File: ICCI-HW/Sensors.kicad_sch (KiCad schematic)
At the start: 20 parts

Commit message: usb PD started
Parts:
- R? (x2): value R -> 4.7k
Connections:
- net +3V3: no longer C?.1, C?.1
- net GND: now also U?.3 (GND), U?.5 (PGND)
- net SCL: now also U?.2 (SCL)
- net SDA: now also U?.8 (SDA)
- net +1V8: now reaches U?.1 (VDD)
- net +1V8: now also C?.1, C?.1
- no-connect marks 0 -> 2
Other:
- note added: "SDA, SCL, INT, LDR are 3V3 tolerant"
- note removed: "1.8V !!!"
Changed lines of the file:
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@@
   (junction (at 161.925 70.485) (diameter 0) (color 0 0 0 0)
   )
+  (junction (at 169.545 95.885) (diameter 0) (color 0 0 0 0)
+  )
   (junction (at 151.13 141.605) (diameter 0) (color 0 0 0 0)
   )
@@
   (junction (at 166.37 80.01) (diameter 0) (color 0 0 0 0)
   )
+  (junction (at 166.37 93.345) (diameter 0) (color 0 0 0 0)
+  )
   (junction (at 134.62 98.425) (diameter 0) (color 0 0 0 0)
   )
+  (junction (at 134.62 120.65) (diameter 0) (color 0 0 0 0)
+  )
+  (no_connect (at 156.21 113.03))
+  (no_connect (at 156.21 110.49))
   (wire (pts (xy 161.925 70.485) (xy 161.925 47.625))
     (stroke (width 0) (type default) (color 0 0 0 0))
@@
     (stroke (width 0) (type default) (color 0 0 0 0))
   )
+  (wire (pts (xy 135.89 120.65) (xy 134.62 120.65))
+    (stroke (width 0) (type default) (color 0 0 0 0))
+  )
   (wire (pts (xy 166.37 59.055) (xy 168.275 59.055))
     (stroke (width 0) (type default) (color 0 0 0 0))
@@
     (stroke (width 0) (type default) (color 0 0 0 0))
   )
+  (wire (pts (xy 156.21 115.57) (xy 166.37 115.57))
+    (stroke (width 0) (type default) (color 0 0 0 0))
+  )
   (wire (pts (xy 166.37 80.01) (xy 161.925 80.01))
     (stroke (width 0) (type default) (color 0 0 0 0))
@@
     (stroke (width 0) (type default) (color 0 0 0 0))
   )
+  (wire (pts (xy 166.37 115.57) (xy 166.37 93.345))
+    (stroke (width 0) (type default) (color 0 0 0 0))
+  )
+  (wire (pts (xy 134.62 118.11) (xy 134.62 120.65))
+    (stroke (width 0) (type default) (color 0 0 0 0))
+  )
   (wire (pts (xy 156.21 73.025) (xy 159.385 73.025))
     (stroke (width 0) (type default) (color 0 0 0 0))
@@
     (stroke (width 0) (type default) (color 0 0 0 0))
   )
+  (wire (pts (xy 134.62 115.57) (xy 135.89 115.57))
+    (stroke (width 0) (type default) (color 0 0 0 0))
+  )
   (wire (pts (xy 151.13 140.97) (xy 151.13 141.605))
     (stroke (width 0) (type default) (color 0 0 0 0))
@@
     (stroke (width 0) (type default) (color 0 0 0 0))
   )
+  (wire (pts (xy 169.545 118.11) (xy 169.545 95.885))
+    (stroke (width 0) (type default) (color 0 0 0 0))
+  )
+  (wire (pts (xy 134.62 114.935) (xy 134.62 115.57))
+    (stroke (width 0) (type default) (color 0 0 0 0))
+  )
   (wire (pts (xy 135.89 75.565) (xy 134.62 75.565))
     (stroke (width 0) (type default) (color 0 0 0 0))
@@
     (stroke (width 0) (type default) (color 0 0 0 0))
   )
+  (wire (pts (xy 135.89 118.11) (xy 134.62 118.11))
+    (stroke (width 0) (type default) (color 0 0 0 0))
+  )
   (wire (pts (xy 147.32 141.605) (xy 151.13 141.605))
     (stroke (width 0) (type default) (color 0 0 0 0))
@@
     (stroke (width 0) (type default) (color 0 0 0 0))
   )
+  (wire (pts (xy 134.62 120.65) (xy 134.62 121.285))
+    (stroke (width 0) (type default) (color 0 0 0 0))
+  )
   (wire (pts (xy 168.275 57.785) (xy 168.275 59.055))
     (stroke (width 0) (type default) (color 0 0 0 0))
@@
     (stroke (width 0) (type default) (color 0 0 0 0))
   )
+  (wire (pts (xy 156.21 118.11) (xy 169.545 118.11))
+    (stroke (width 0) (type default) (color 0 0 0 0))
+  )
   (wire (pts (xy 156.21 50.165) (xy 159.385 50.165))
     (stroke (width 0) (type default) (color 0 0 0 0))
@@
     (stroke (width 0) (type default) (color 0 0 0 0))
   )
-  (text "RGB + C" (at 182.88 46.355 0)
+  (text "RGB + C" (at 175.895 48.895 0)
     (effects (font (size 1.27 1.27)) (justify left bottom))
   )
-  (text "C" (at 184.785 73.025 0)
+  (text "C" (at 178.435 71.755 0)
     (effects (font (size 1.27 1.27)) (justify left bottom))
   )
-  (text "IR + IR&C" (at 184.785 94.615 0)
+  (text "IR + IR&C" (at 173.99 93.98 0)
+    (effects (font (size 1.27 1.27)) (justify left bottom))
+  )
+  (text "SDA, SCL, INT, LDR are 3V3 tolerant" (at 131.445 129.54 0)
     (effects (font (size 1.27 1.27)) (justify left bottom))
   )
@@
   (text "SENSORS" (at 147.955 33.02 180)
     (effects (font (size 3 3) (thickness 0.6) bold) (justify right bottom))
-  )
-  (text "1.8V !!!" (at 164.465 114.935 0)
-    (effects (font (size 1.27 1.27)) (justify left bottom))
   )
   (global_label "DQ" (shape bidirectional) (at 175.26 141.605 0) (fields_autoplaced)
@@
     (pin "1")
   )
-  (symbol (lib_id "power:+3V3") (at 118.745 113.03 0) (unit 1)
+  (symbol (lib_id "power:+1V8") (at 118.745 113.03 0) (unit 1)
     (in_bom yes) (on_board yes)
     (property "Reference" "#PWR?" (id 0) (at 118.745 116.84 0)
       (effects (font (size 1.27 1.27)) hide)
     )
-    (property "Value" "+3V3" (id 1) (at 118.745 109.22 0))
+    (property "Value" "+1V8" (id 1) (at 118.11 109.22 0))
     (property "Footprint" "" (id 2) (at 118.745 113.03 0)
       (effects (font (size 1.27 1.27)) hide)
@@
   (symbol (lib_id "Device:R") (at 166.37 73.66 0) (unit 1)
     (in_bom yes) (on_board yes)
-    (property "Reference" "R?" (id 0) (at 162.56 72.39 0)
-      (effects (font (size 1.27 1.27)) (justify left))
-    )
-    (property "Value" "R" (id 1) (at 162.56 74.93 0)
+    (property "Reference" "R?" (id 0) (at 163.83 69.85 0)
+      (effects (font (size 1.27 1.27)) (justify left))
+    )
+    (property "Value" "4.7k" (id 1) (at 163.83 75.565 90)
       (effects (font (size 1.27 1.27)) (justify left))
     )
@@
     (pin "1")
   )
+  (symbol (lib_id "power:GND") (at 134.62 121.285 0) (unit 1)
+    (in_bom yes) (on_board yes) (fields_autoplaced)
+    (property "Reference" "#PWR?" (id 0) (at 134.62 127.635 0)
+      (effects (font (size 1.27 1.27)) hide)
+    )
+    (property "Value" "GND" (id 1) (at 134.62 125.73 0))
+    (property "Footprint" "" (id 2) (at 134.62 121.285 0)
+      (effects (font (size 1.27 1.27)) hide)
+    )
+    (property "Datasheet" "" (id 3) (at 134.62 121.285 0)
+      (effects (font (size 1.27 1.27)) hide)
+    )
+    (pin "1")
+  )
   (symbol (lib_id "power:GND") (at 118.745 76.835 0) (unit 1)
     (in_bom yes) (on_board yes)
@@
     (pin "1")
     (pin "2")
+  )
+  (symbol (lib_id "power:+1V8") (at 134.62 114.935 0) (unit 1)
+    (in_bom yes) (on_board yes)
+    (property "Reference" "#PWR?" (id 0) (at 134.62 118.745 0)
+      (effects (font (size 1.27 1.27)) hide)
+    )
+    (property "Value" "+1V8" (id 1) (at 133.985 111.125 0))
+    (property "Footprint" "" (id 2) (at 134.62 114.935 0)
+      (effects (font (size 1.27 1.27)) hide)
+    )
+    (property "Datasheet" "" (id 3) (at 134.62 114.935 0)
+      (effects (font (size 1.27 1.27)) hide)
+    )
+    (pin "1")
   )
   (symbol (lib_id "power:+3V3") (at 118.745 69.215 0) (unit 1)
@@
     (pin "2")
   )
-  (symbol (lib_id "power:+3V3") (at 125.095 113.03 0) (unit 1)
+  (symbol (lib_id "power:+1V8") (at 125.095 113.03 0) (unit 1)
     (in_bom yes) (on_board yes)
     (property "Reference" "#PWR?" (id 0) (at 125.095 116.84 0)
       (effects (font (size 1.27 1.27)) hide)
     )
-    (property "Value" "+3V3" (id 1) (at 125.095 109.22 0))
+    (property "Value" "+1V8" (id 1) (at 124.46 109.22 0))
     (property "Footprint" "" (id 2) (at 125.095 113.03 0)
       (effects (font (size 1.27 1.27)) hide)
@@
   )
   (symbol (lib_id "Device:R") (at 169.545 73.66 0) (unit 1)
-    (in_bom yes) (on_board yes) (fields_autoplaced)
-    (property "Reference" "R?" (id 0) (at 172.085 72.3899 0)
-      (effects (font (size 1.27 1.27)) (justify left))
-    )
-    (property "Value" "R" (id 1) (at 172.085 74.9299 0)
-      (effects (font (size 1.27 1.27)) (justify left))
-    )
+    (in_bom yes) (on_board yes)
+    (property "Reference" "R?" (id 0) (at 170.18 69.85 0)
+      (effects (font (size 1.27 1.27)) (justify left))
+    )
+    (property "Value" "4.7k" (id 1) (at 172.085 75.565 90)
+      (effects (font (size 1.27 1.27)) (justify left))
+    )

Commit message: updated
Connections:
- net DQ renamed DS_DQ
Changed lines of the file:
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@@
     (stroke (width 0) (type default) (color 0 0 0 0))
   )
-  (wire (pts (xy 151.13 141.605) (xy 175.26 141.605))
+  (wire (pts (xy 151.13 141.605) (xy 172.085 141.605))
     (stroke (width 0) (type default) (color 0 0 0 0))
   )
@@
     (effects (font (size 3 3) (thickness 0.6) bold) (justify right bottom))
   )
-  (global_label "DQ" (shape bidirectional) (at 175.26 141.605 0) (fields_autoplaced)
+  (hierarchical_label "SDA" (shape bidirectional) (at 173.99 82.55 0)
     (effects (font (size 1.27 1.27)) (justify left))
-    (property "Intersheet References" "${INTERSHEET_REFS}" (id 0) (at 180.2736 141.5256 0)
-      (effects (font (size 1.27 1.27)) (justify left) hide)
-    )
   )
-  (global_label "SCL" (shape input) (at 173.99 80.01 0) (fields_autoplaced)
+  (hierarchical_label "SCL" (shape input) (at 173.99 80.01 0)
     (effects (font (size 1.27 1.27)) (justify left))
-    (property "Intersheet References" "${INTERSHEET_REFS}" (id 0) (at 179.9107 79.9306 0)
-      (effects (font (size 1.27 1.27)) (justify left) hide)
-    )
   )
-  (global_label "SDA" (shape bidirectional) (at 173.99 82.55 0) (fields_autoplaced)
+  (hierarchical_label "DS_DQ" (shape bidirectional) (at 172.085 141.605 0)
     (effects (font (size 1.27 1.27)) (justify left))
-    (property "Intersheet References" "${INTERSHEET_REFS}" (id 0) (at 179.9712 82.4706 0)
-      (effects (font (size 1.27 1.27)) (justify left) hide)
-    )
   )
   (symbol (lib_id "power:GND") (at 125.095 53.975 0) (unit 1)

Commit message: updated
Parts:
- removed JP? (x2): SolderJumper_2_Bridged, symbol Jumper:SolderJumper_2_Bridged
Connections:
- net +3V3: now also R?.1, R?.1
- net SCL renamed SCL0
- net SDA renamed SDA0
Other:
- moved on the sheet: R?

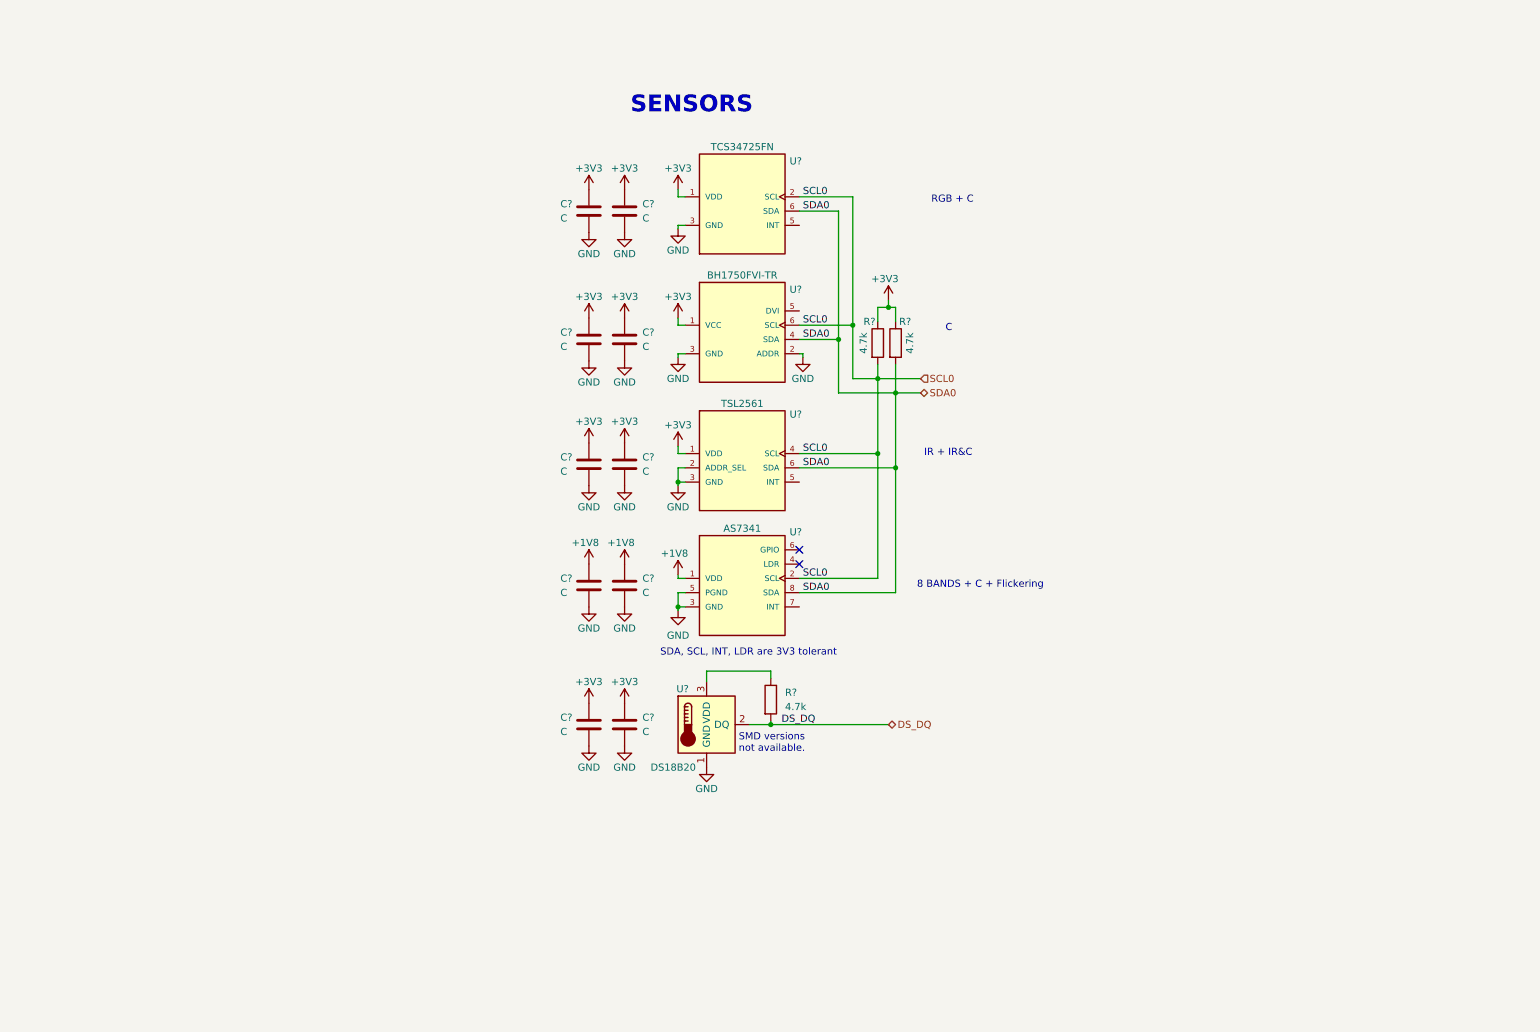
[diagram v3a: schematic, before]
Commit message: add GPIO Expansion
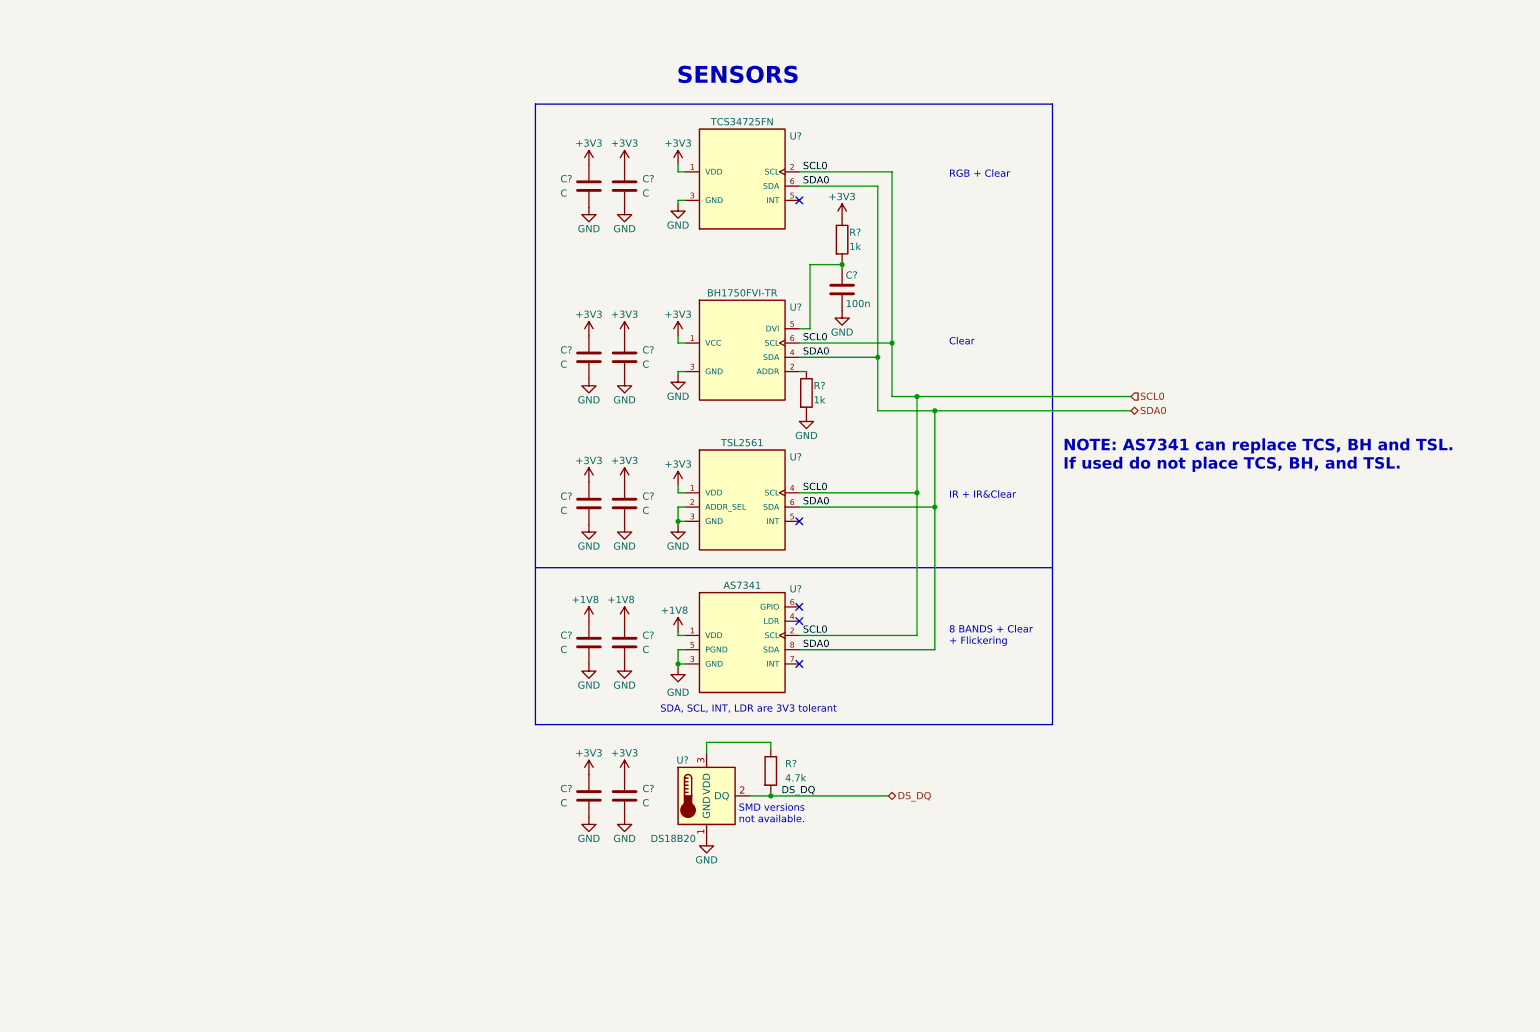
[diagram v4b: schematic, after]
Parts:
- removed R? (x2): 4.7k, symbol Device:R
- added C?: 100n, symbol Device:C
- added R? (x2): 1k, symbol Device:R
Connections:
- net +3V3: now also R?.1
- net GND: now also C?.2, R?.2; no longer U?.2 (ADDR)
- net at U?.5 (DVI): now also C?.1, R?.2
- new net: R?.1, U?.2 (ADDR)
- no-connect marks 2 -> 5
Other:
- note added: "8 BANDS + Clear + Flickering"
- note added: "Clear"
- note added: "IR + IR&Clear"
- note added: "NOTE: AS7341 can replace TCS, BH and TSL. If used do not place TCS, BH, and TSL."
- note added: "RGB + Clear"
- note removed: "8 BANDS + C + Flickering"
- note removed: "C"
- note removed: "IR + IR&C"
- note removed: "RGB + C"
- moved on the sheet: C?, R?, U?

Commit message: updated
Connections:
- net +3V3: now also R?.1, U?.3 (VDD)
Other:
- note added: "NOTE: DS18B20 Driver is using RMT ESP peripheral in order to properly handle OneWire bus without bit banding (available via IO MUX through every GPIO pin)"
- moved on the sheet: C?, R?, U?

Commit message: schematic V1.0
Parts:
- C301: renamed from C?; value C -> 4,7u
- C302, C303, C304, C305: renamed from C?; value C -> 1u
- C306, C307, C308, C309, C310: renamed from C?; value C -> 100n
- gave numbers to parts that had none: 9

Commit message: footprint assigned
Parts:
- C301, C302, C303, C304, C305, C306, C307, C308, C309, C310, C311: footprint (none) -> Capacitor_SMD:C_0603_1608Metric
- R301, R302, R303: footprint (none) -> Resistor_SMD:R_0603_1608Metric
- U302: footprint (none) -> ICCI-LIB:BH1750FVI-TR
- U303: footprint (none) -> ICCI-LIB:TCS34725FN
- U304: footprint (none) -> ICCI-LIB:TLS2561
- U305: footprint (none) -> ICCI-LIB:AS7431
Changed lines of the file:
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@@
       (effects (font (size 1.27 1.27)) (justify left))
     )
-    (property "Footprint" "" (id 2) (at 69.342 76.835 90)
+    (property "Footprint" "Resistor_SMD:R_0603_1608Metric" (id 2) (at 69.342 76.835 90)
       (effects (font (size 1.27 1.27)) hide)
     )
@@
     (property "Reference" "U303" (id 0) (at 70.485 31.115 0))
     (property "Value" "TCS34725FN" (id 1) (at 59.69 28.575 0))
-    (property "Footprint" "" (id 2) (at 59.69 37.465 0)
+    (property "Footprint" "ICCI-LIB:TCS34725FN" (id 2) (at 59.69 37.465 0)
       (effects (font (size 1.27 1.27)) (justify left bottom) hide)
     )
@@
       (effects (font (size 1.27 1.27)) (justify left))
     )
-    (property "Footprint" "" (id 2) (at 39.7002 125.095 0)
+    (property "Footprint" "Capacitor_SMD:C_0603_1608Metric" (id 2) (at 39.7002 125.095 0)
       (effects (font (size 1.27 1.27)) hide)
     )
@@
       (effects (font (size 1.27 1.27)) (justify left))
     )
-    (property "Footprint" "" (id 2) (at 33.3502 100.33 0)
+    (property "Footprint" "Capacitor_SMD:C_0603_1608Metric" (id 2) (at 33.3502 100.33 0)
       (effects (font (size 1.27 1.27)) hide)
     )
@@
       (effects (font (size 1.27 1.27)) (justify left))
     )
-    (property "Footprint" "" (id 2) (at 33.3502 74.295 0)
+    (property "Footprint" "Capacitor_SMD:C_0603_1608Metric" (id 2) (at 33.3502 74.295 0)
       (effects (font (size 1.27 1.27)) hide)
     )
@@
       (effects (font (size 1.27 1.27)) (justify left))
     )
-    (property "Footprint" "" (id 2) (at 75.692 49.53 90)
+    (property "Footprint" "Resistor_SMD:R_0603_1608Metric" (id 2) (at 75.692 49.53 90)
       (effects (font (size 1.27 1.27)) hide)
     )
@@
       (effects (font (size 1.27 1.27)) (justify left))
     )
-    (property "Footprint" "" (id 2) (at 39.7002 43.815 0)
+    (property "Footprint" "Capacitor_SMD:C_0603_1608Metric" (id 2) (at 39.7002 43.815 0)
       (effects (font (size 1.27 1.27)) hide)
     )
@@
       (effects (font (size 1.27 1.27)) (justify left))
     )
-    (property "Footprint" "" (id 2) (at 39.7002 74.295 0)
+    (property "Footprint" "Capacitor_SMD:C_0603_1608Metric" (id 2) (at 39.7002 74.295 0)
       (effects (font (size 1.27 1.27)) hide)
     )
@@
     (property "Reference" "U305" (id 0) (at 70.485 111.76 0))
     (property "Value" "AS7341" (id 1) (at 59.69 111.125 0))
-    (property "Footprint" "" (id 2) (at 62.23 125.095 0)
+    (property "Footprint" "ICCI-LIB:AS7431" (id 2) (at 62.23 125.095 0)
       (effects (font (size 1.27 1.27)) (justify left bottom) hide)
     )
@@
       (effects (font (size 1.27 1.27)) (justify left))
     )
-    (property "Footprint" "" (id 2) (at 39.0652 156.21 0)
+    (property "Footprint" "Capacitor_SMD:C_0603_1608Metric" (id 2) (at 39.0652 156.21 0)
       (effects (font (size 1.27 1.27)) hide)
     )
@@
       (effects (font (size 1.27 1.27)) (justify left))
     )
-    (property "Footprint" "" (id 2) (at 39.7002 100.33 0)
+    (property "Footprint" "Capacitor_SMD:C_0603_1608Metric" (id 2) (at 39.7002 100.33 0)
       (effects (font (size 1.27 1.27)) hide)
     )
@@
       (effects (font (size 1.27 1.27)) (justify left))
     )
-    (property "Footprint" "" (id 2) (at 62.357 147.955 90)
+    (property "Footprint" "Resistor_SMD:R_0603_1608Metric" (id 2) (at 62.357 147.955 90)
       (effects (font (size 1.27 1.27)) hide)
     )
@@
       (effects (font (size 1.27 1.27)) (justify left))
     )
-    (property "Footprint" "" (id 2) (at 78.4352 62.23 0)
+    (property "Footprint" "Capacitor_SMD:C_0603_1608Metric" (id 2) (at 78.4352 62.23 0)
       (effects (font (size 1.27 1.27)) hide)
     )
@@
       (effects (font (size 1.27 1.27)) (justify left))
     )
-    (property "Footprint" "" (id 2) (at 32.7152 156.21 0)
+    (property "Footprint" "Capacitor_SMD:C_0603_1608Metric" (id 2) (at 32.7152 156.21 0)
       (effects (font (size 1.27 1.27)) hide)
     )
@@
     (property "Reference" "U302" (id 0) (at 59.055 80.01 0))
     (property "Value" "BH1750FVI-TR" (id 1) (at 59.69 59.055 0))
-    (property "Footprint" "" (id 2) (at 67.31 70.485 0)
+    (property "Footprint" "ICCI-LIB:BH1750FVI-TR" (id 2) (at 67.31 70.485 0)
       (effects (font (size 1.27 1.27)) (justify left bottom) hide)
     )
@@
     (property "Reference" "U304" (id 0) (at 70.485 88.265 0))
     (property "Value" "TSL2561" (id 1) (at 59.69 85.725 0))
-    (property "Footprint" "" (id 2) (at 59.69 97.155 0)
+    (property "Footprint" "ICCI-LIB:TLS2561" (id 2) (at 59.69 97.155 0)
       (effects (font (size 1.27 1.27)) (justify left bottom) hide)
     )
@@
       (effects (font (size 1.27 1.27)) (justify left))
     )
-    (property "Footprint" "" (id 2) (at 33.3502 125.095 0)
+    (property "Footprint" "Capacitor_SMD:C_0603_1608Metric" (id 2) (at 33.3502 125.095 0)
       (effects (font (size 1.27 1.27)) hide)
     )
@@
       (effects (font (size 1.27 1.27)) (justify left))
     )
-    (property "Footprint" "" (id 2) (at 33.3502 43.815 0)
-      (effects (font (size 1.27 1.27)) hide)
-    )
+    (property "Footprint" "Capacitor_SMD:C_0603_1608Metric" (id 2) (at 33.3502 43.815 0)
+      (effects (font (size 1.27 1.27)) hide)
+    )
